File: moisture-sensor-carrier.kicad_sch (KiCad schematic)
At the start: 56 parts, among them J1 USB-C receptacle, J2 Battery 503450 + NTC, J3 Solar panel, J4 SWD 10p 1.27mm, J5 Antenna feed, U1 nRF54L15-QFAA, U2 nPM1300-QEAA, U3 FDC1004, U4 SHT45-AD1F, X1 CM8V-T1A 32.768kHz CL=7pF 20p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, X2 32MHz CL=8pF 40ppm

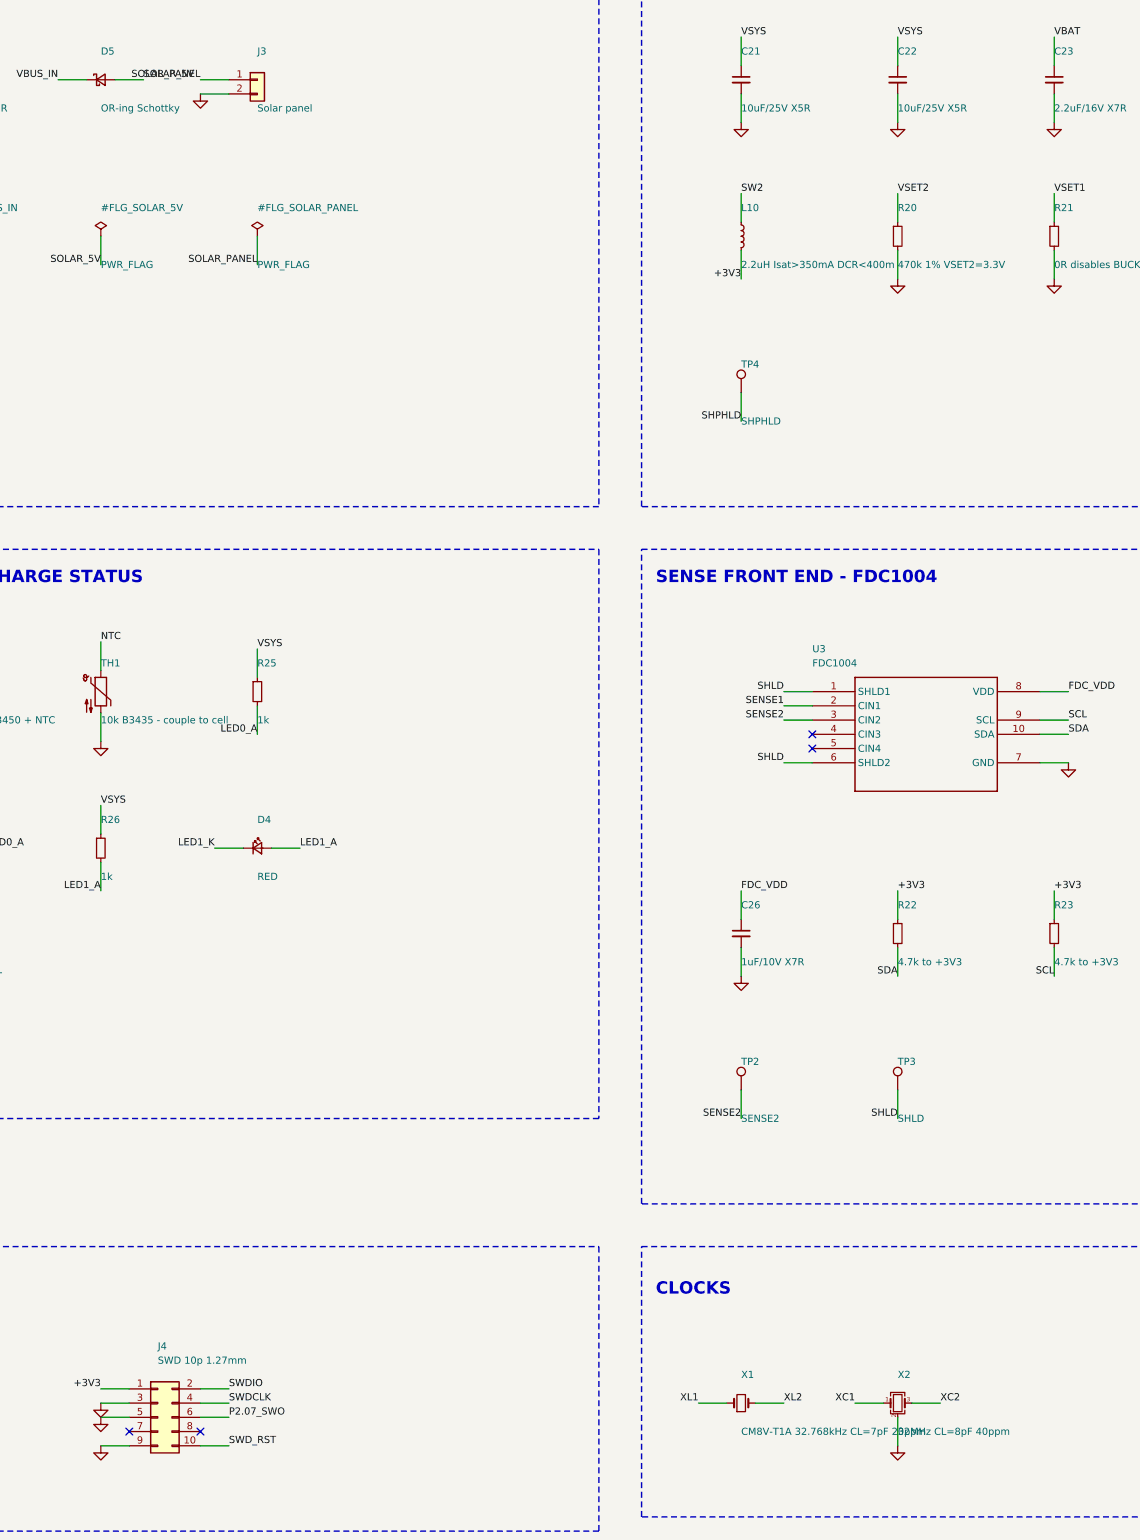
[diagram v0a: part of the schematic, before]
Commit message: D5 = Panjit RB751V-40; X2 = Epson FA-128 8 pF
D5: 370 mV at 1 mA, 300 mA, 40 V reverse, 500 nA leakage, SOD-323,
$0.14. Chosen over BAT201M3, which has a lower drop (290 mV at 10 mA)
and 1 A rating but only 20 V reverse - thin against the 22 V VBUS abs max
that HARDWARE.md section 4 leans on - and 50 uA leakage. Recorded two
traps from the same search: RB751V-40WS and RB751V-40X share the 370 mV
figure but are rated 30 mA not 300, and BAS70WS/BAT42WS/BAT43WS all quote
1 V forward.

X2: 2016 was never a requirement, only Nordic's reference BOM. The
datasheet characterises 2.0x1.6 and 1.2x1.0 and mandates neither - the
small one passes at 100 ohm ESR because its C0 is 0.42 pF. C0 and ESR
trade on the Figure 17 curve; package size is a proxy.

FA-128 totals 25 ppm (12 initial + 12 temp over -20..+75 C + 1 aging)
against a 40 ppm requirement, where the ABM11A's best combination was 48.
ESR 60 ohm max at 32 MHz sits under the ~100 ohm the CL=8pF curve allows
at C0 0.74 pF. Two things to close: Epson does not publish C0, and their
recommended land pattern does not match KiCad's generic 2016 footprint -
the same mismatch that forced a vendor footprint for X1.

Co-Authored-By: Claude Opus 5 <noreply@anthropic.com>
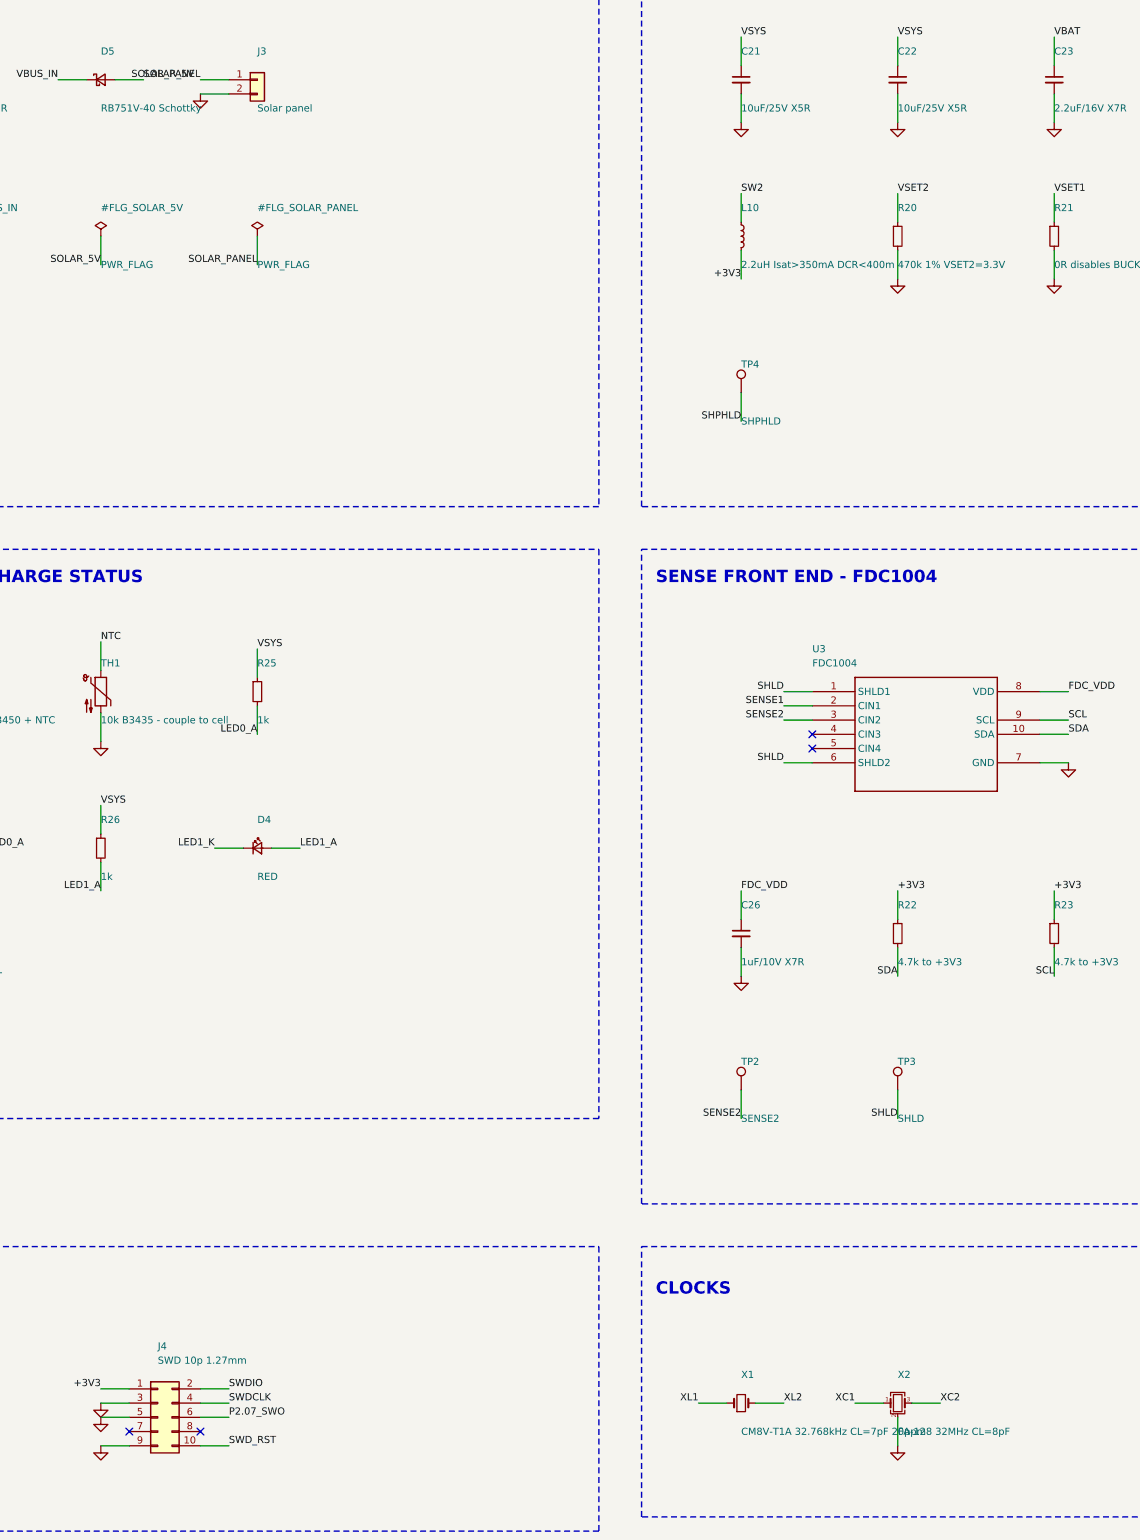
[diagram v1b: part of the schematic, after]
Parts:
- D5: value OR-ing Schottky -> RB751V-40 Schottky
- X2: value 32MHz CL=8pF 40ppm -> FA-128 32MHz CL=8pF
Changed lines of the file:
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@@
 			(effects (font (size 1.27 1.27)) (justify left))
 		)
-		(property "Value" "OR-ing Schottky"
+		(property "Value" "RB751V-40 Schottky"
 			(at 60.96 111.76 0)
 			(effects (font (size 1.27 1.27)) (justify left))
@@
 			(effects (font (size 1.27 1.27)) (justify left))
 		)
-		(property "Value" "32MHz CL=8pF 40ppm"
+		(property "Value" "FA-128 32MHz CL=8pF"
 			(at 203.2 347.98 0)
 			(effects (font (size 1.27 1.27)) (justify left))

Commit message: Cell = Adafruit 1578 (500 mAh); J2 = 2-pin JST PH
Cell drops from the 258 to the 1578 for fit margin. The 258 is 34.0 mm
across a 34.92 mm interior and its part code (503562) implies a 35 mm
nominal cell that would not go in at all; pouch cells also swell. 1578 is
29 mm across, 6 mm of slack, at a cost of 0.5 years (2.9 vs 3.45).

J2 becomes a 2-pin JST PH so an Adafruit cell plugs straight in. Drops the
pack-NTC pin, which costs nothing - Adafruit cells are 2-wire with no
thermistor, so the NTC path was always TH1.

PH is 8 mm against 6.90 mm of clearance under the cell, so tools_gen_pcb.py
now models the cell footprint and asserts that anything in COMPONENT_HEIGHTS
taller than the gap sits outside it. The cell covers 36 mm of the 74 mm
board, so the y 62-74 band keeps the full 11.70 mm and J2 goes there.

Power budget rescaled to 500 mAh. Worth noting the balance shifts: self
discharge falls from 92% of the budget on the 2000 mAh cell to 74% here,
and the PCM's quiescent current is now 16% - twice the whole nRF+PMIC
sleep draw. Measuring it matters more than it did.

Co-Authored-By: Claude Opus 5 <noreply@anthropic.com>
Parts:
- removed J2: Battery 503450 + NTC, Connector_JST:JST_GH_SM03B-GHS-TB_1x03-1MP_P1.25mm_Horizontal, symbol Connector_Generic:Conn_01x03
- added J2: Battery - Adafruit 1578, Connector_JST:JST_PH_B2B-PH-K_1x02_P2.00mm_Vertical, symbol Connector_Generic:Conn_01x02
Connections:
- net GND: now also J2.2 (Pin_2)
- net VBAT: now also J2.1 (Pin_1)
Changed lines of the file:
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@@
-		(stroke (width 0) (type default))
-	)
-	(wire (pts (xy 27.940000000000005 213.36) (xy 22.860000000000007 213.36))
 		(stroke (width 0) (type default))
 	)
@@
 	)
 	(label "VBAT"
-		(at 22.860000000000007 213.36 0)
-		(fields_autoplaced yes)
-		(effects (font (size 1.27 1.27)) (justify right bottom))
-	)
-	(label "NTC"
 		(at 22.860000000000007 215.9 0)
 		(fields_autoplaced yes)
@@
 	)
 	(symbol
-		(lib_id "Connector_Generic:Conn_01x03")
+		(lib_id "Connector_Generic:Conn_01x02")
 		(at 33.02 215.9 0)
 		(unit 1)
@@
 			(effects (font (size 1.27 1.27)) (justify left))
 		)
-		(property "Value" "Battery 503450 + NTC"
+		(property "Value" "Battery - Adafruit 1578"
 			(at 33.02 220.98 0)
 			(effects (font (size 1.27 1.27)) (justify left))
 		)
-		(property "Footprint" "Connector_JST:JST_GH_SM03B-GHS-TB_1x03-1MP_P1.25mm_Horizontal"
+		(property "Footprint" "Connector_JST:JST_PH_B2B-PH-K_1x02_P2.00mm_Vertical"
 			(at 33.02 215.9 0)
 			(effects (font (size 1.27 1.27)) (hide yes))
@@
 		(pin "1")
 		(pin "2")
-		(pin "3")
-		(instances
-			(project "moisture-sensor-carrier"
+		(instances
+			(project "moisture-sensor-carrier"

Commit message: X2 land pattern; split the enclosure model into lid/bottom/gasket
X2 moves to an Epson-specific footprint. Their recommended land is
0.50 x 0.85 mm pads on 0.95 (X) by 1.15 (Y) centres, a 1.45 x 2.00 mm
envelope. KiCad's generic Crystal_SMD_2016-4Pin uses 0.90 x 0.80 pads on
1.40 x 1.10 centres - a 2.30 mm outer span, 0.85 mm wider than Epson
specify. Pads 1/3 are the crystal terminals, 2/4 the metal cover to
ground, matching the existing netlist.

Hammond ship the 1551WK as a STEP assembly, not one solid. Split with
OCCT into Bottom, Lid and Gasket, each with its own show flag, positions
preserved from the assembly:
  Bottom  y  0.00 - 16.91
  Lid     y 16.00 - 22.00
  Gasket  y 16.42 - 17.62

Those numbers answer the question directly: the PCB is not sandwiched
between the halves and is not the gasket. It sits on 4.00 mm posts inside
the bottom, top face at y = 5.60, about 11 mm below the gasket seam. The
seal is a separate silicone part.

Caveat: the split files are valid STEP with correct geometry, but
kicad-cli's renderer will not draw them while it does draw Hammond's
combined .stp. ENCL_SPLIT = False falls back to the combined model.

Co-Authored-By: Claude Opus 5 <noreply@anthropic.com>
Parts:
- X2: footprint Crystal:Crystal_SMD_2016-4Pin_2.0x1.6mm -> footprints:XTAL_FA-128_2016_4Pin
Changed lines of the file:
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@@
 			(effects (font (size 1.27 1.27)) (justify left))
 		)
-		(property "Footprint" "Crystal:Crystal_SMD_2016-4Pin_2.0x1.6mm"
+		(property "Footprint" "footprints:XTAL_FA-128_2016_4Pin"
 			(at 203.2 342.9 0)
 			(effects (font (size 1.27 1.27)) (hide yes))
